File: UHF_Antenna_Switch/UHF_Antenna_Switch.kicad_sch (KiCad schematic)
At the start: 0 parts

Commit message: Schematic: Draw relays and dummy load
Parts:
- added J1: Conn_Feedline, symbol Connector:Conn_Coaxial
- added J2: Conn_Uplink, symbol Connector:Conn_Coaxial
- added J3: Conn_Downlink, symbol Connector:Conn_Coaxial
- added K1, K2: HF3-51, Relay_SMD:Relay_SPDT_AXICOM_HF3Series_50ohms_Pitch1.27mm, symbol Relay:HF3-51
- added R1: R, symbol Device:R
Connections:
- new net: K1.14, K2.14
- new net: J3.1 (In), K1.20
- new net: J1.1 (In), K1.6
- new net: K2.20, R1.1
- new net: J2.1 (In), K2.6
- new net GNDD: K1.11, K2.11
- new net GNDS: J1.2 (Ext), J2.2 (Ext), J3.2 (Ext), K1.10 (GND), K1.12 (GND), K1.13 (GND), K1.15 (GND), K1.17 (GND), K1.19 (GND), K1.2 (GND), K1.21 (GND), K1.22 (GND), K1.5 (GND), K1.7 (GND), K2.10 (GND), K2.12 (GND), K2.13 (GND), K2.15 (GND), K2.17 (GND), K2.19 (GND), K2.2 (GND), K2.21 (GND), K2.22 (GND), K2.5 (GND), K2.7 (GND), R1.2
- new net TX_EN_RELAY_CTRL_K1: K1.1
- new net TX_EN_RELAY_CTRL_K2: K2.1
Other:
- note added: "RF Dummy Load"
- note added: "RF Relays and Dummy Load"

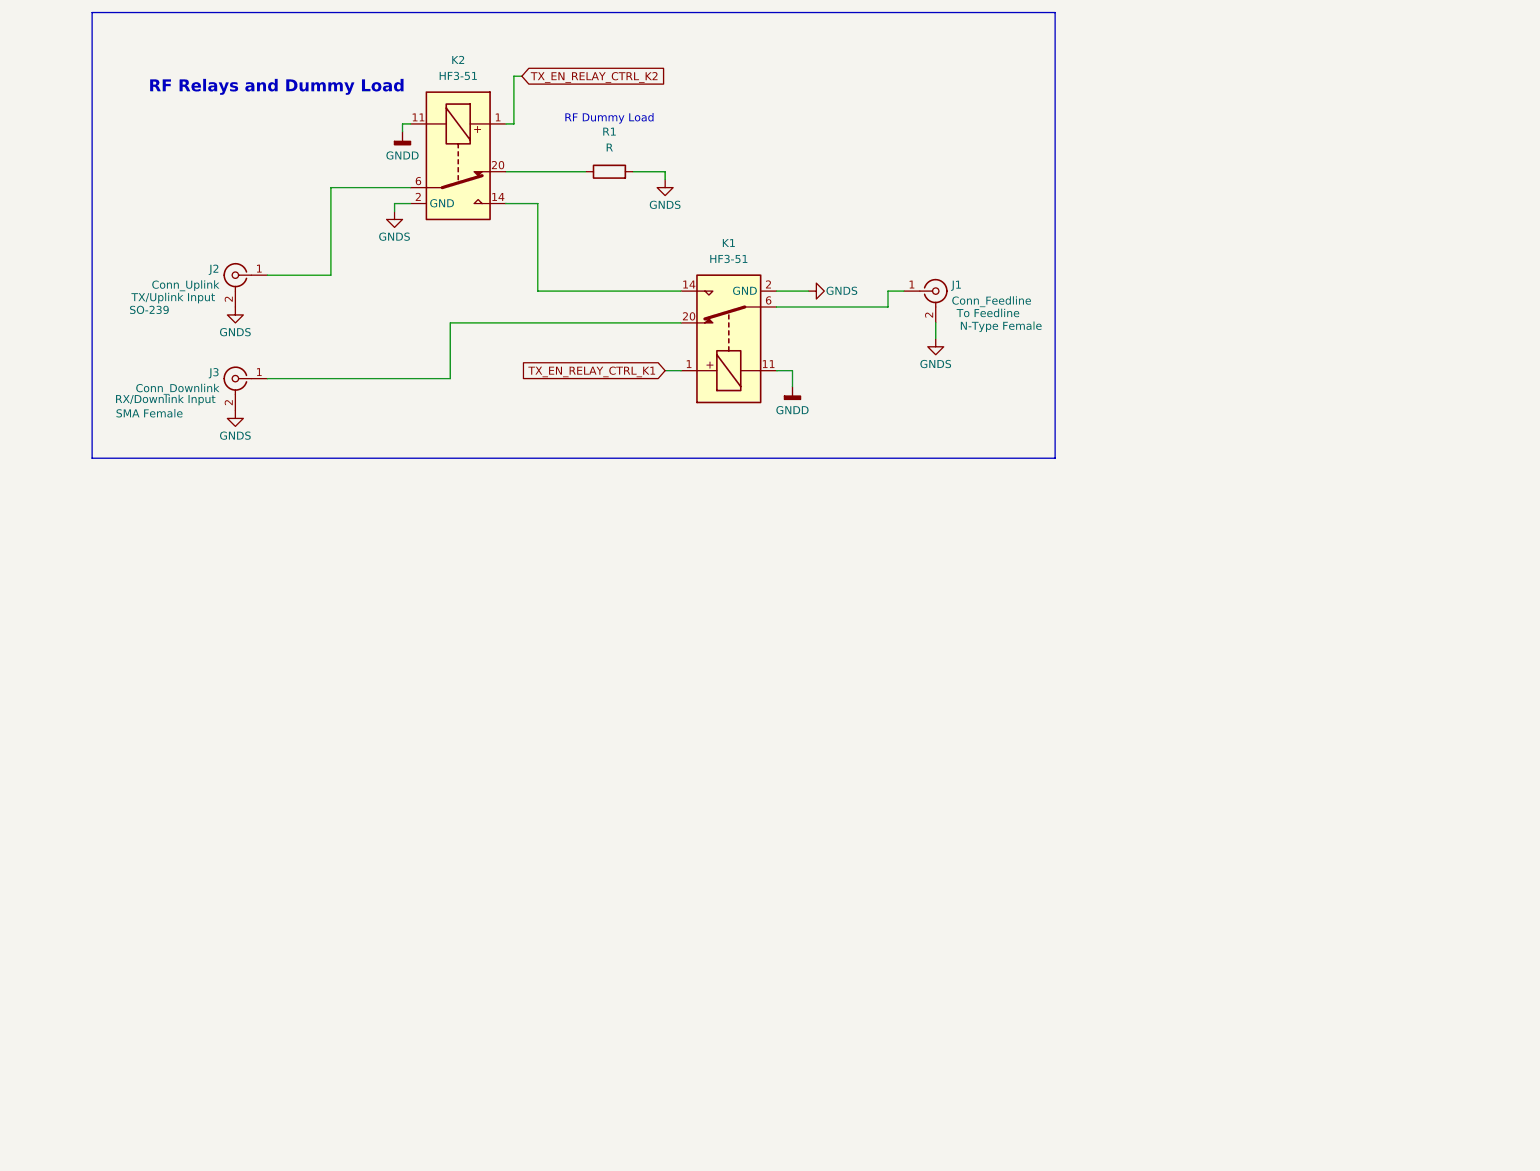
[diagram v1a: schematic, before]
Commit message: Draw relay buffers and detector
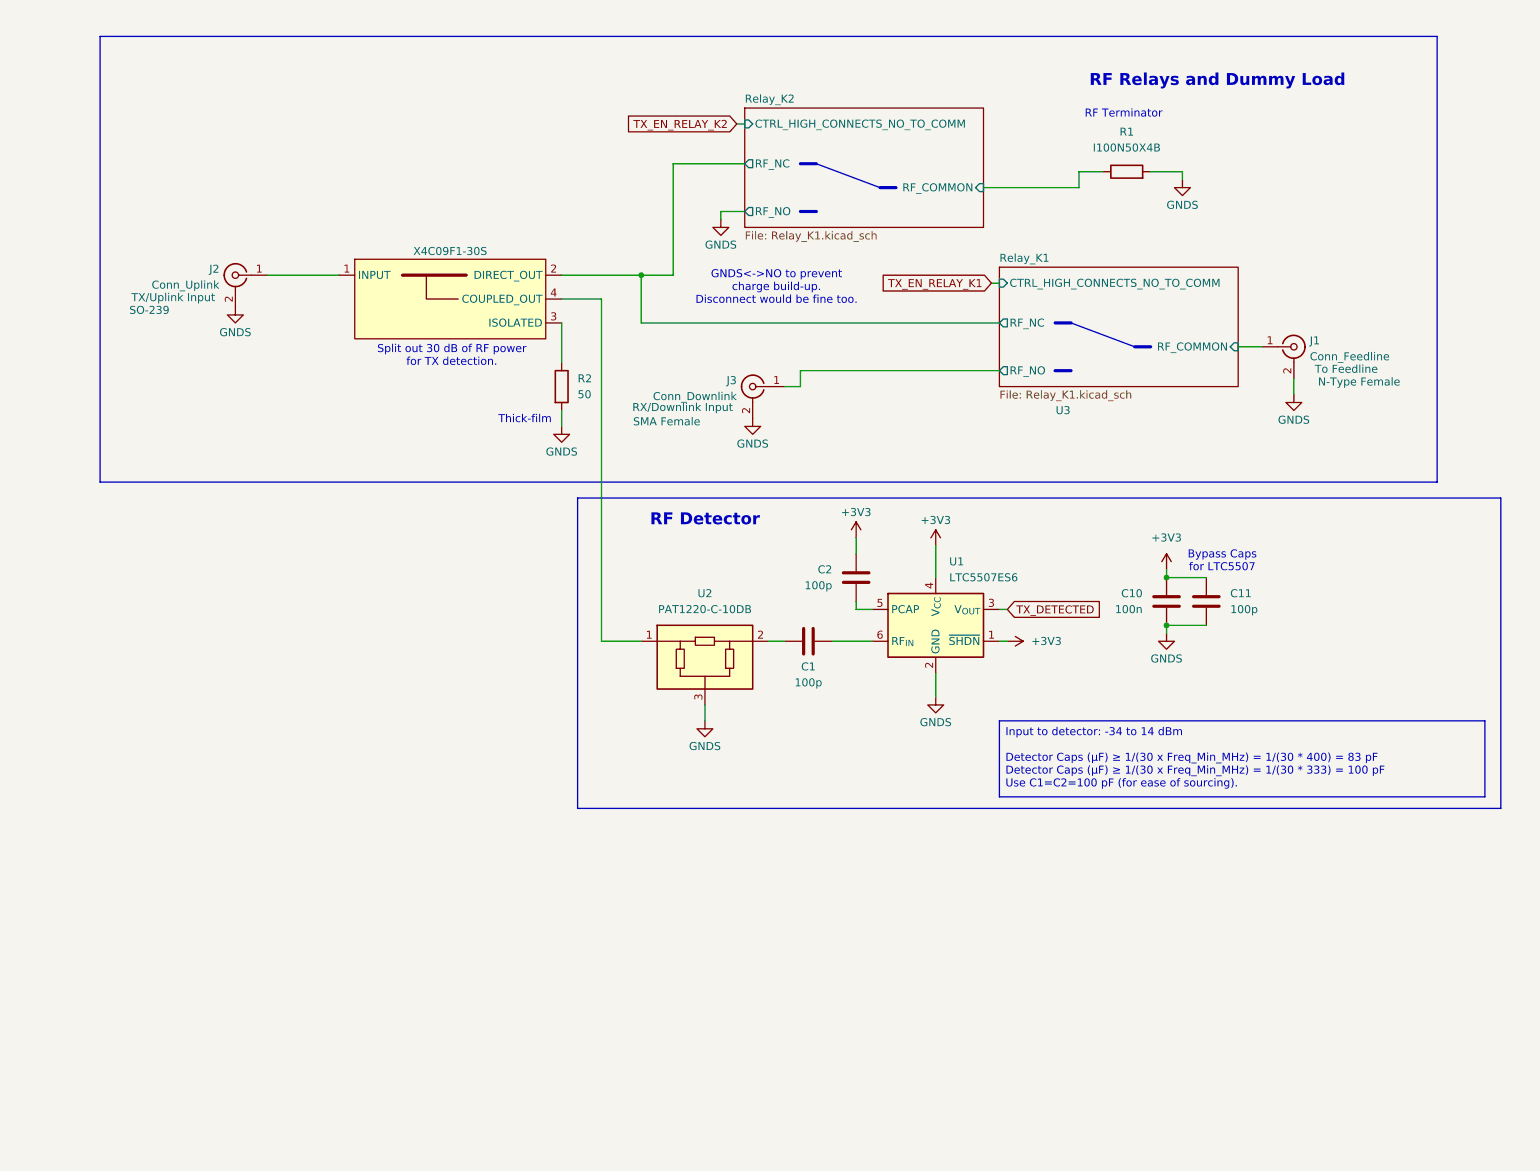
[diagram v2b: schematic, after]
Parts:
- removed K1, K2: HF3-51, Relay_SMD:Relay_SPDT_AXICOM_HF3Series_50ohms_Pitch1.27mm, symbol Relay:HF3-51
- added C1, C11, C2: 100p, symbol Device:C
- added C10: 100n, symbol Device:C
- added R2: 50, symbol Device:R
- added U1: LTC5507ES6, Package_TO_SOT_SMD:TSOT-23-6_HandSoldering, symbol RF:LTC5507ES6
- added U2: PAT1220-C-10DB, RF_Converter:RF_Attenuator_Susumu_PAT1220, symbol RF:PAT1220-C-10DB
- added U3: X4C09F1-30S, symbol 00-project-symbols:X4C09F1-30S
- R1: value R -> I100N50X4B
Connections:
- net GNDS: now also C10.2, C11.2, R2.2, U1.2 (GND), U2.3
- net Relay_K1/RF_NO: now reaches J3.1 (In)
- net Relay_K1/RF_COMMON: now reaches J1.1 (In)
- net Relay_K2/RF_COMMON: now reaches R1.1
- net at J2.1 (In): now also U3.1 (INPUT)
- new net: U2.1, U3.4 (COUPLED_OUT)
- new net: C1.1, U2.2
- new net: C1.2, U1.6 (RF_{IN})
- new net: C2.2, U1.5 (PCAP)
- new net: R2.1, U3.3 (ISOLATED)
- new net +3V3: C10.1, C11.1, C2.1, U1.1 (~{SHDN}), U1.4 (V_{CC})
- new net Relay_K1/RF_NC: U3.2 (DIRECT_OUT)
- new net TX_DETECTED: U1.3 (V_{OUT})
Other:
- added sheet Relay_K1 (Relay_K1.kicad_sch)
- added sheet Relay_K2 (Relay_K1.kicad_sch)
- note added: "Bypass Caps for LTC5507"
- note added: "GNDS<->NO to prevent charge build-up. Disconnect would be fine too."
- note added: "RF Detector"
- note added: "RF Terminator"
- note added: "Split out 30 dB of RF power for TX detection."
- note added: "Thick-film"
- note removed: "RF Dummy Load"
- moved on the sheet: J1, J3, R1

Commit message: Schematic: Add RP2040 microcontroller and LEDs
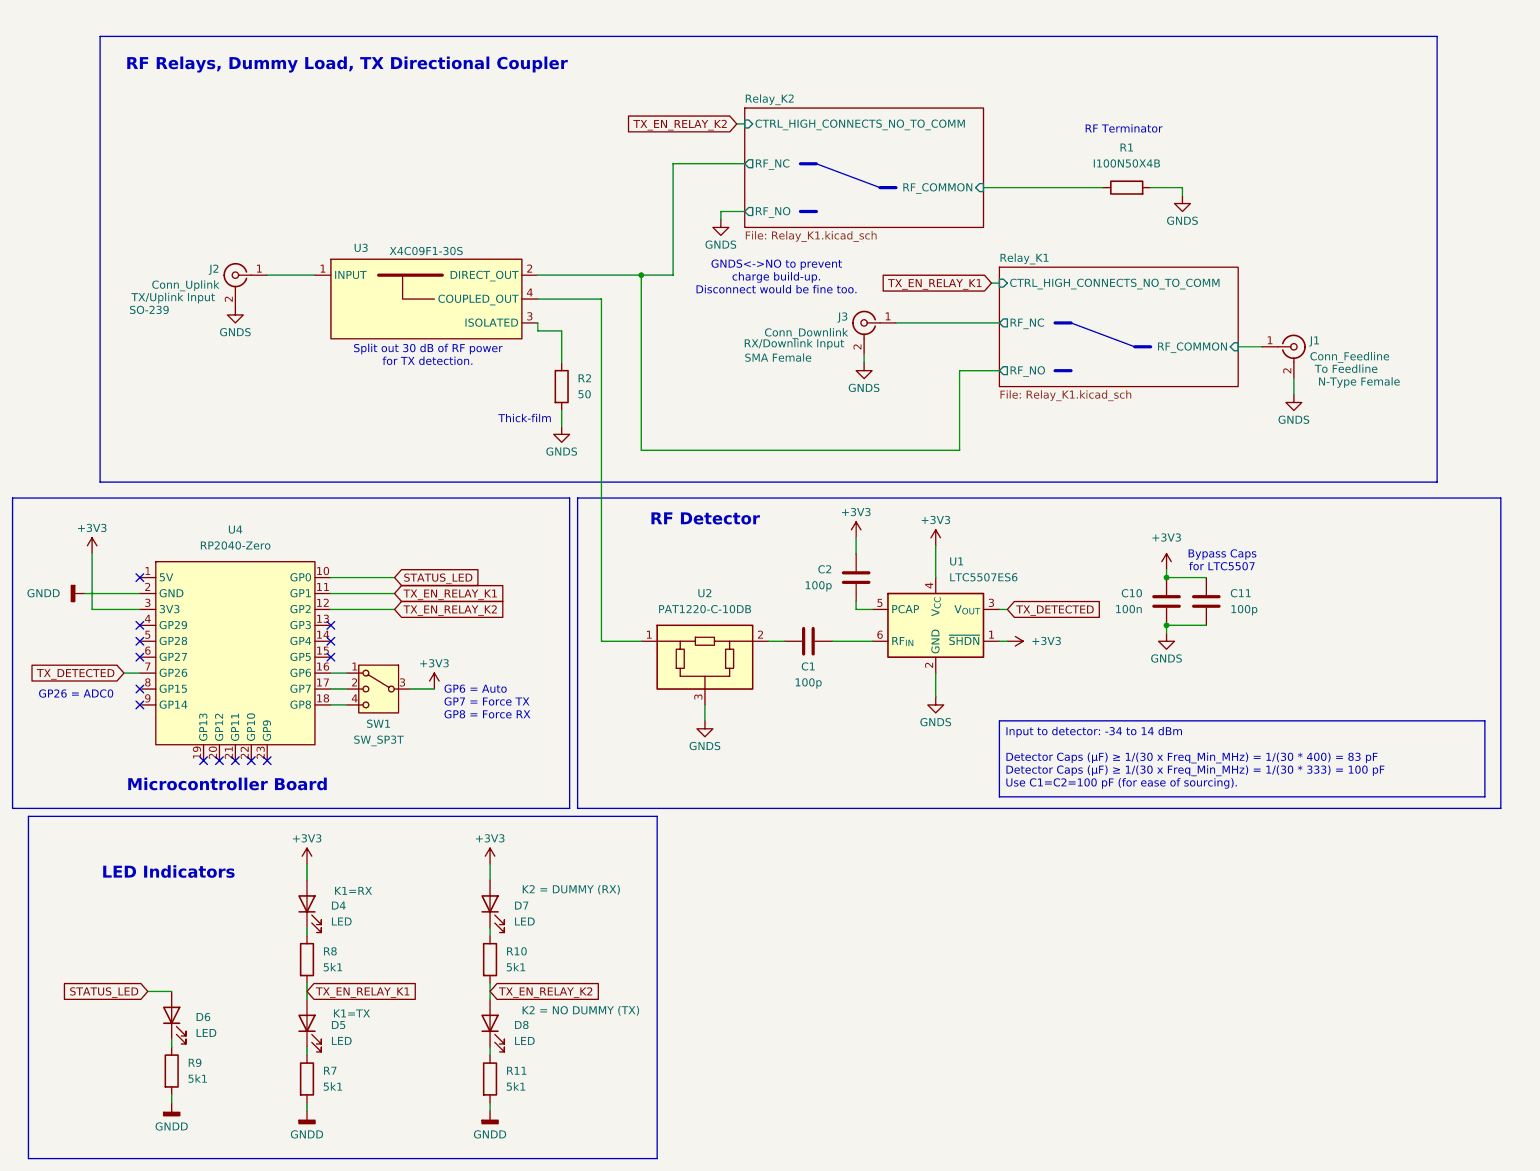
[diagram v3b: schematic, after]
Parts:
- added D4, D5, D6, D7, D8: LED, symbol Device:LED
- added R10, R11, R7, R8, R9: 5k1, symbol Device:R
- added SW1: SW_SP3T, symbol Switch:SW_SP3T
- added U4: RP2040-Zero, 00-project-footprints:RP2040 Zero, symbol 00-project-symbols:RP2040-Zero
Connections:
- net +3V3: now also D4.2 (A), D7.2 (A), SW1.3, U4.3 (3V3)
- net Relay_K1/RF_NC: now also J3.1 (In); no longer U3.2 (DIRECT_OUT)
- net Relay_K1/RF_NO: now also U3.2 (DIRECT_OUT); no longer J3.1 (In)
- net TX_DETECTED: now also U4.7 (GP26)
- net TX_EN_RELAY_K1: now also D5.2 (A), R8.2, U4.11 (GP1)
- net TX_EN_RELAY_K2: now also D8.2 (A), R10.2, U4.12 (GP2)
- new net: D4.1 (K), R8.1
- new net: D5.1 (K), R7.1
- new net: D6.1 (K), R9.1
- new net: D8.1 (K), R11.1
- new net: D7.1 (K), R10.1
- new net: SW1.1, U4.16 (GP6)
- new net: SW1.2, U4.17 (GP7)
- new net: SW1.4, U4.18 (GP8)
- new net GNDD: R11.2, R7.2, R9.2, U4.2 (GND)
- new net STATUS_LED: D6.2 (A), U4.10 (GP0)
- no-connect marks 0 -> 14
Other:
- note added: "GP26 = ADC0"
- note added: "GP6 = Auto GP7 = Force TX GP8 = Force RX"
- note added: "LED Indicators"
- note added: "Microcontroller Board"
- note added: "RF Relays, Dummy Load, TX Directional Coupler"
- note removed: "RF Relays and Dummy Load"
- moved on the sheet: J3, R1, U3

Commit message: Assign most footprints
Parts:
- added D9: LED, LED_SMD:LED_0603_1608Metric_Pad1.05x0.95mm_HandSolder, symbol Device:LED
- added R12: 5k1, Resistor_SMD:R_0603_1608Metric_Pad0.98x0.95mm_HandSolder, symbol Device:R
- C1, C10, C11, C2: footprint (none) -> Capacitor_SMD:C_0603_1608Metric_Pad1.08x0.95mm_HandSolder
- D4, D5, D6, D7, D8: footprint (none) -> LED_SMD:LED_0603_1608Metric_Pad1.05x0.95mm_HandSolder
- J1: value Conn_Feedline -> Conn_SMA_Female; footprint (none) -> Connector_Coaxial:SMA_Amphenol_901-143_Horizontal; Connector Type N-Type Female -> To N-Type Female
- J2: value Conn_Uplink -> Conn_SMA_Female; footprint (none) -> Connector_Coaxial:SMA_Amphenol_901-143_Horizontal; Connector Type SO-239 -> To SO-239 Female
- J3: value Conn_Downlink -> Conn_SMA_Female; footprint (none) -> Connector_Coaxial:SMA_Amphenol_901-143_Horizontal
- R10, R11, R2, R7, R8, R9: footprint (none) -> Resistor_SMD:R_0603_1608Metric_Pad0.98x0.95mm_HandSolder
- SW1: footprint (none) -> Button_Switch_SMD:SW_SP3T_PCM13
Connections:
- net +3V3: now also D9.2 (A)
- net GNDD: now also R12.2
- new net: D9.1 (K), R12.1

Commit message: Add N-Type PCB connector footprint
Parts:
- J1: value Conn_SMA_Female -> Conn_N_Type_Female; footprint Connector_Coaxial:SMA_Amphenol_901-143_Horizontal -> 00-project-footprints:Amphenol N Jack 172234; Connector Type To N-Type Female -> N-Type Female
- J2: value Conn_SMA_Female -> Conn_SO-239; footprint Connector_Coaxial:SMA_Amphenol_901-143_Horizontal -> 00-project-footprints:Amphenol N Jack 172234; Connector Type To SO-239 Female -> SO-239 Female
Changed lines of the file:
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@@
 			)
 		)
-		(property "Value" "Conn_SMA_Female"
+		(property "Value" "Conn_N_Type_Female"
 			(at 220.98 70.1431 0)
 			(show_name no)
@@
 			)
 		)
-		(property "Footprint" "Connector_Coaxial:SMA_Amphenol_901-143_Horizontal"
+		(property "Footprint" "00-project-footprints:Amphenol N Jack 172234"
 			(at 218.44 68.58 0)
 			(hide yes)
@@
 			)
 		)
-		(property "Connector Type" "To N-Type Female"
-			(at 230.378 74.168 0)
+		(property "Connector Type" "N-Type Female"
+			(at 228.854 74.168 0)
 			(show_name no)
 			(do_not_autoplace no)
@@
 			)
 		)
-		(property "Value" "Conn_SMA_Female"
+		(property "Value" "Conn_SO-239"
 			(at 46.99 58.7131 0)
 			(show_name no)
@@
 			)
 		)
-		(property "Footprint" "Connector_Coaxial:SMA_Amphenol_901-143_Horizontal"
+		(property "Footprint" "00-project-footprints:Amphenol N Jack 172234"
 			(at 49.53 57.15 0)
 			(hide yes)
@@
 			)
 		)
-		(property "Connector Type" "To SO-239 Female"
+		(property "Connector Type" "SO-239 Female"
 			(at 39.116 62.992 0)
 			(show_name no)

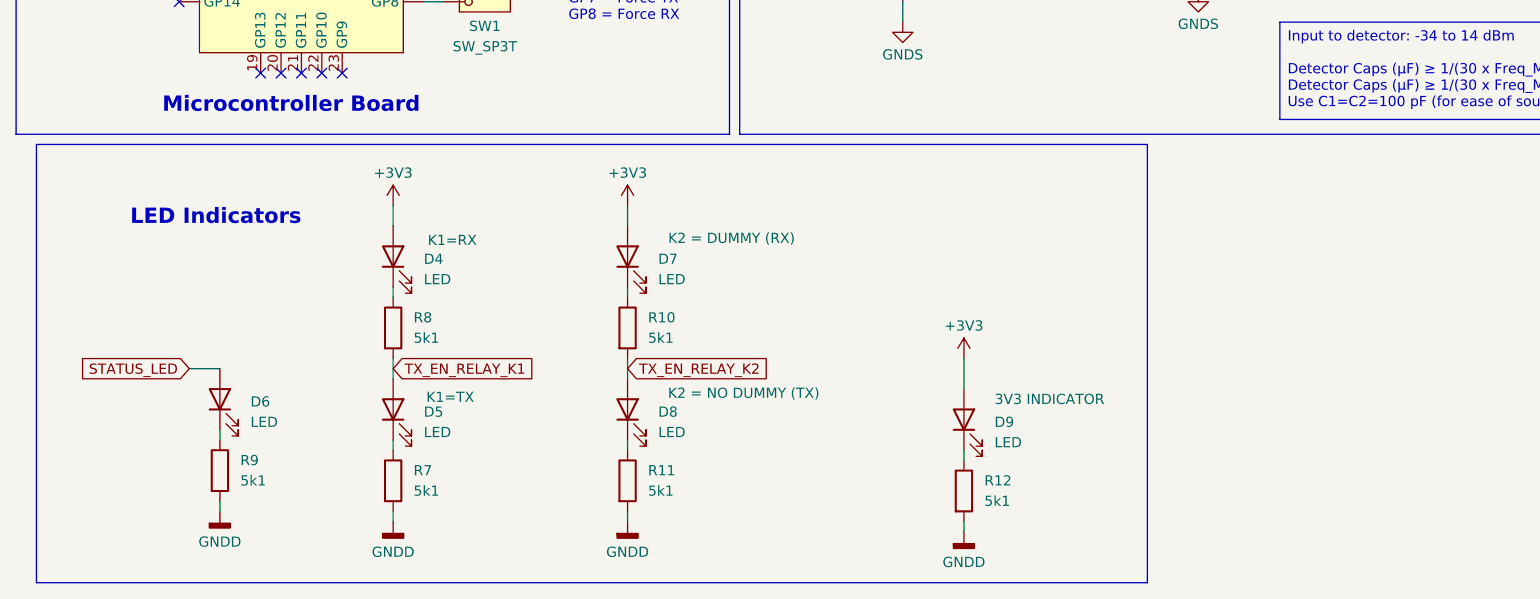
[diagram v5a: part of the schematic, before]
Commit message: Add 3V3 power connector
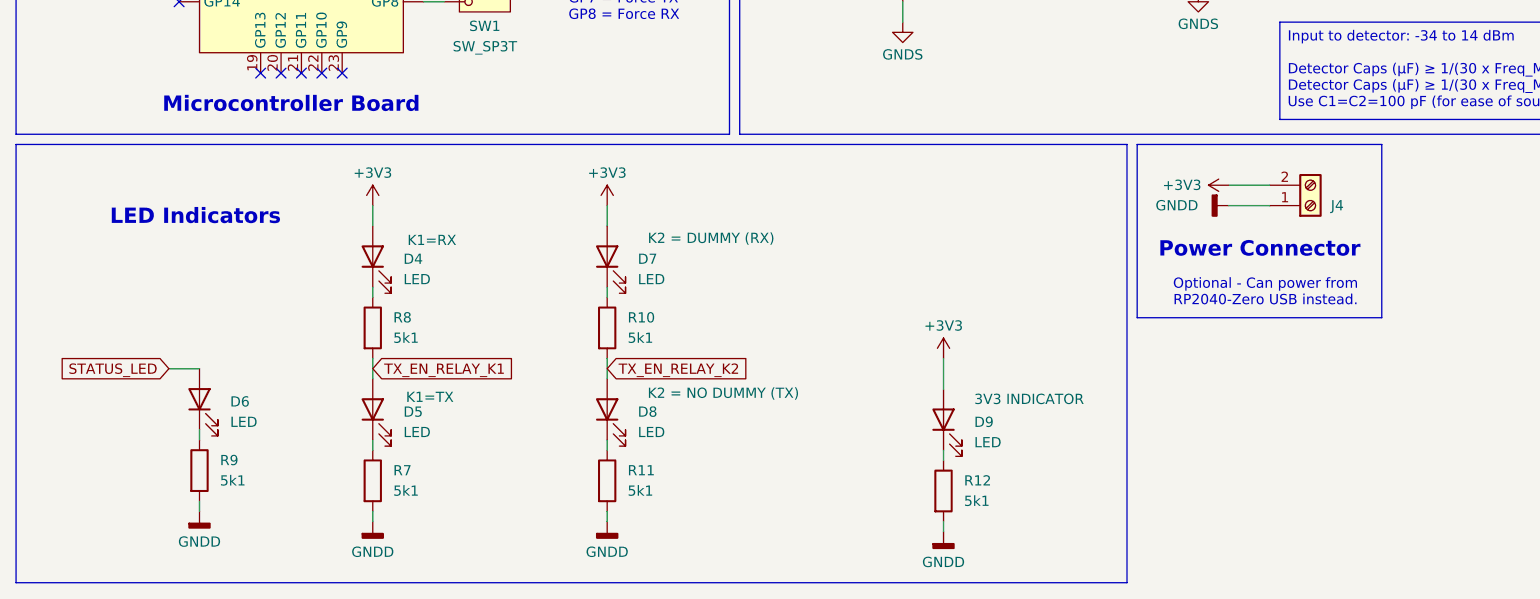
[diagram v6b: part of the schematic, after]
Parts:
- added J4: Screw_Terminal_01x02, TerminalBlock_Phoenix:TerminalBlock_Phoenix_MKDS-3-2-5.08_1x02_P5.08mm_Horizontal, symbol Connector:Screw_Terminal_01x02
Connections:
- net +3V3: now also J4.2 (Pin_2)
- net GNDD: now also J4.1 (Pin_1)
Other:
- note added: "Optional - Can power from RP2040-Zero USB instead."
- note added: "Power Connector"
- moved on the sheet: D4, D5, D6, D7, D8, D9, R10, R11, R12, R7, R8, R9
